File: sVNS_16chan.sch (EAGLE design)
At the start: 7 parts, among them IC1 EFM8SB10F8G-A-CSP16R, IC2 OPA990IDCKR, U1 NT3H2211W0FHKH, U2 LT8410EDC-1#TRMPBF, U3 MUX36S16IRSNR, U4 MUX36S16IRSNR

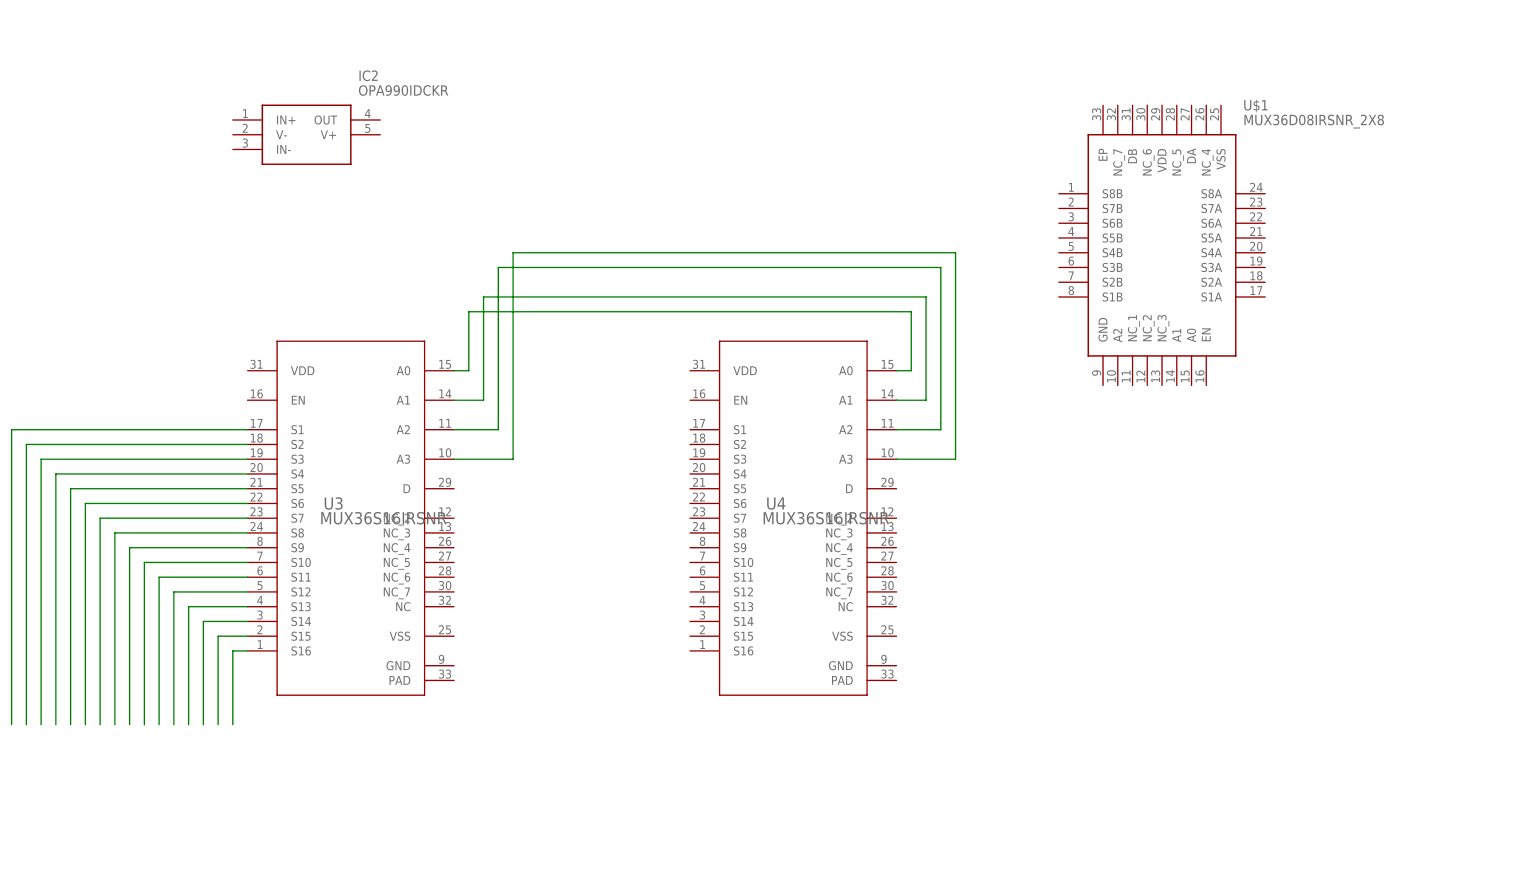
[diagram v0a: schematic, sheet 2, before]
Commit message: Draft of 2x MUX36S16 for output and 1x MUX36D08 for H-bridge
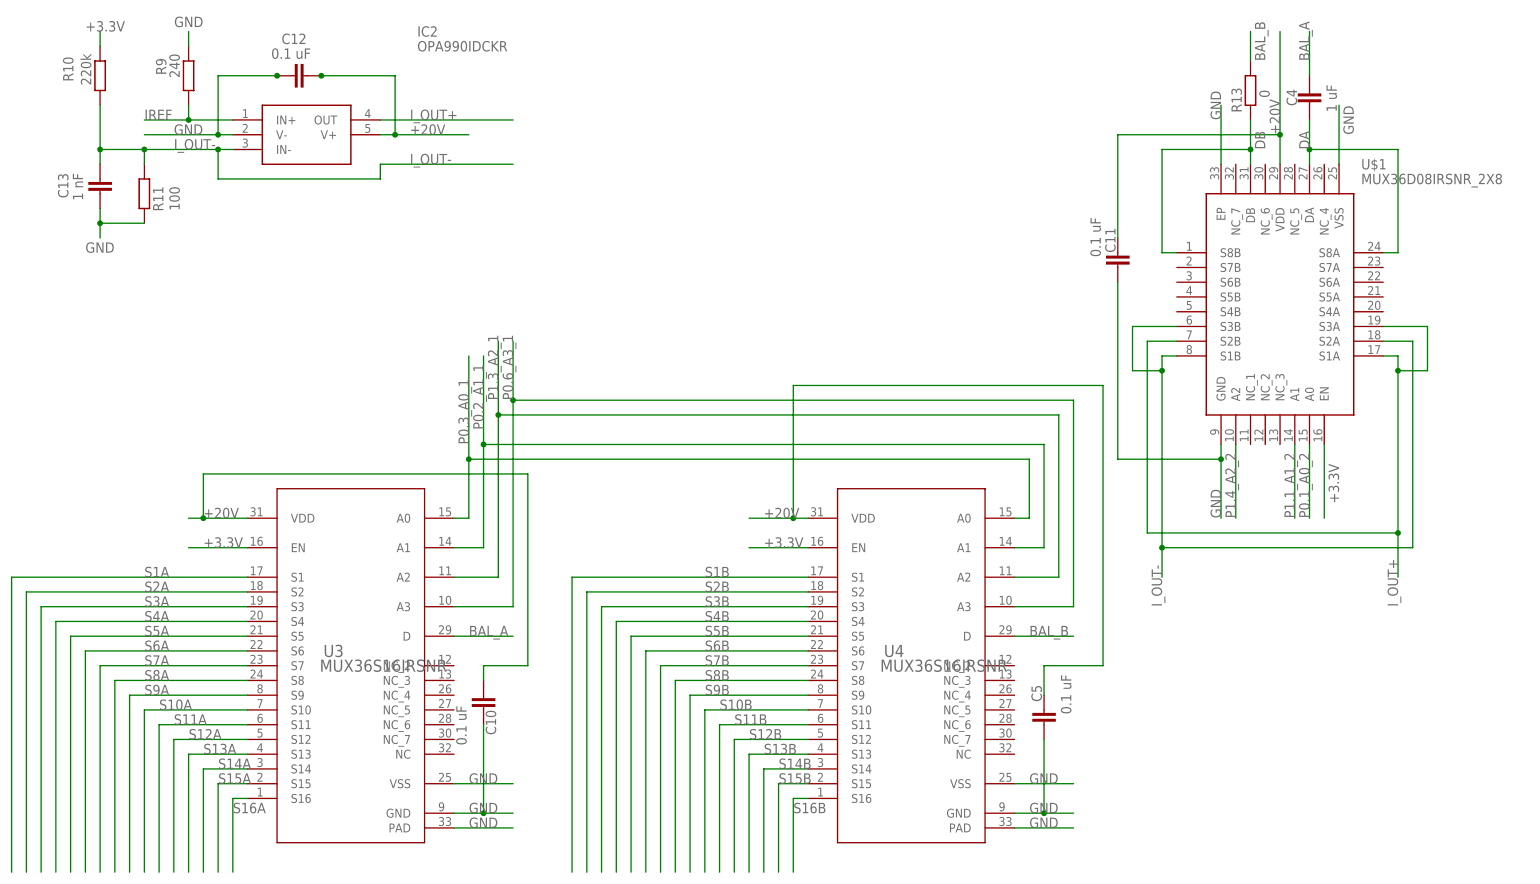
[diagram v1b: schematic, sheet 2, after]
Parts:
- added +20V_EXTERNAL_POWER: +20V external, pinhead:PINHD-1X2
- added +3.3V_EXTERNAL_POWER: +3.3V external, pinhead:PINHD-1X2
- added ANTENNA: Antenna connector, pinhead:PINHD-1X2
- added C1, C3: 2.2 uF, rcl:C-EUC0402
- added C10, C11, C12, C2, C5, C7: 0.1 uF, rcl:C-EUC0402
- added C13: 1 nF, rcl:C-EUC0402
- added C4, C8: 1 uF, rcl:C-EUC0402
- added C6: 82p, rcl:C-EUC0402
- added C9: 0.22u, rcl:C-EUC0402
- added L1: 47 uH, CustomLibVNS:0603PS-473KRC0603PS
- added R1: 487k, rcl:R-EU_R0603
- added R10: 220k, rcl:R-EU_R0402
- added R11: 100, rcl:R-EU_R0402
- added R13: 0, rcl:R-EU_R0402
- added R2: 511k, rcl:R-EU_R0603
- added R3: 1.3M, rcl:R-EU_R0402
- added R4: 100k, rcl:R-EU_R0402
- added R5, R6, R7: 10k, rcl:R-EU_R0402
- added R8: 1k, rcl:R-EU_R0402
- added R9: 240, rcl:R-EU_R0402
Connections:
- net N$1 renamed S16A
- net N$10 renamed S7A
- net N$11 renamed S6A
- net N$12 renamed S5A
- net N$13 renamed S4A
- net N$14 renamed S3A
- net N$15 renamed S2A
- net N$16 renamed S1A
- net N$2 renamed S15A
- net N$3 renamed S14A
- net N$4 renamed S13A
- net N$5 renamed S12A
- net N$6 renamed S11A
- net N$7 renamed S10A
- net N$8 renamed S9A
- net N$9 renamed S8A
- removed net N$17: U3.A0, U4.A0
- removed net N$18: U3.A1, U4.A1
- removed net N$19: U3.A2, U4.A2
- removed net N$20: U3.A3, U4.A3
- new net +20V: +20V_EXTERNAL_POWER.1, C10.1, C11.2, C3.1, C5.2, IC2.V+, U$1.VDD, U2.VOUT, U3.VDD, U4.VDD
- new net +20V1: C12.1
- new net +3.3V: +3.3V_EXTERNAL_POWER.1, C1.2, C7.2, C8.1, C9.1, IC1.VDD, L1.1, R10.1, R5.2, R6.2, R7.2, R8.1, U$1.EN, U1.VCC, U1.VOUT, U2.VCC, U3.EN, U4.EN
- new net BAL_A: C4.2, U3.D
- new net BAL_B: R13.2, U4.D
- new net DA: C4.1, U$1.DA, U$1.S8A
- new net DB: R13.1, U$1.DB, U$1.S8B
- new net FBP: R1.1, R2.2, U2.FBP
- new net FD: R7.1, U1.FD
- new net GND: +20V_EXTERNAL_POWER.2, +3.3V_EXTERNAL_POWER.2, C1.1, C10.2, C11.1, C13.1, C2.1, C3.2, C5.1, C7.1, C8.2, C9.2, IC1.GND, IC2.V-, R11.2, R2.1, R4.1, R9.1, U$1.EP, U$1.GND, U$1.VSS, U1.VSS, U2.EP, U2.GND, U3.GND, U3.PAD, U3.VSS, U4.GND, U4.PAD, U4.VSS
- new net GND1: C12.2
- new net IREF: IC2.IN+, R9.2
- new net I_OUT+: IC2.OUT, R3.2, U$1.S1A, U$1.S2B, U$1.S3A
- new net I_OUT-: C13.2, IC2.IN-, R10.2, R11.1, U$1.S1B, U$1.S2A, U$1.S3B
- new net N$56: ANTENNA.1, C6.1, U1.LA
- new net N$57: ANTENNA.2, C6.2, U1.LB
- new net N$58: C2.2, U2.CAP
- new net P0.0_SMBUS_SDA: IC1.P0.0, R5.1, U1.SDA
- new net P0.1_A0_2: IC1.P0.1, U$1.A0
- new net P0.2_A1_1: IC1.P0.2, U3.A1, U4.A1
- new net P0.3_A0_1: IC1.P0.3, U3.A0, U4.A0
- new net P0.4_SMBUS_SCL: IC1.P0.4, R6.1, U1.SCL
- new net P0.5_ADC: IC1.P0.5, R3.1, R4.2
- new net P0.6_A3_1: IC1.P0.6, U3.A3, U4.A3
- new net P0.7_IREF: IC1.P0.7
- new net P1.0_SHDN: IC1.P1.0, U2.!SHDN
- new net P1.1_A1_2: IC1.P1.1, U$1.A1
- new net P1.3_A2_1: IC1.P1.3, U3.A2, U4.A2
- new net P1.4_A2_2: IC1.P1.4, U$1.A2
- new net P2.7_/_C2D: IC1.P2.7_/_C2D
- new net RSTB_/_C2CK: IC1.RSTB_/_C2CK, R8.2
- new net S10B: U4.S10
- new net S11B: U4.S11
- new net S12B: U4.S12
- new net S13B: U4.S13
- new net S14B: U4.S14
- new net S15B: U4.S15
- new net S16B: U4.S16
- new net S1B: U4.S1
- new net S2B: U4.S2
- new net S3B: U4.S3
- new net S4B: U4.S4
- new net S5B: U4.S5
- new net S6B: U4.S6
- new net S7B: U4.S7
- new net S8B: U4.S8
- new net S9B: U4.S9
- new net SW: L1.2, U2.SW
- new net VREF: R1.2, U2.VREF
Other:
- note added: "External power supllies"
- moved on the sheet: IC1, U$1, U3, U4

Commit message: Schematic to submit to Enrico #1
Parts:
- added +20V_CHECK: Converted voltage, pinhead:PINHD-1X2
- added +3.3V_CHECK: Harvested voltage/NT3H, pinhead:PINHD-1X2
- added BAL_A: BAL_A check, pinhead:PINHD-1X2
- added BAL_B: BAL_B check, pinhead:PINHD-1X2
- added DEBUG_N_2510_SOCKET: N2510-6002RB, N2510-6002RB:N2510-6002RB
- added EFM8_VDD: EFM8 check, pinhead:PINHD-1X2
- added GROUND_CONNECTION: GND, pinhead:PINHD-1X2
- added I_OUT+: I_out+ check, pinhead:PINHD-1X2
- added I_OUT-: I_out- check, pinhead:PINHD-1X2
- added I_REF: IREF check, pinhead:PINHD-1X2
- added LT8410_VCC: LT8410 check, pinhead:PINHD-1X2
- added MUX36D08_VDD: MUX36D08 check, pinhead:PINHD-1X2
- added MUX36S16_A, MUX36S16_B: MUX36S16 check, pinhead:PINHD-1X2
- added OPA990_V+: OPA990 check, pinhead:PINHD-1X2
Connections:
- net N$56 renamed LA
- net N$57 renamed LB
- new net N$1: C7.2, C8.1, EFM8_VDD.2, R8.1
- new net N$2: LT8410_VCC.2, U2.VCC
- new net N$3: I_OUT+.2
- new net N$4: I_OUT-.1
- net +20V: now also +20V_CHECK.1, +20V_CHECK.2, MUX36D08_VDD.1, MUX36D08_VDD.2, MUX36S16_A.1, MUX36S16_A.2, MUX36S16_B.1, MUX36S16_B.2, OPA990_V+.1, OPA990_V+.2
- net +3.3V: now also +3.3V_CHECK.1, +3.3V_CHECK.2, EFM8_VDD.1, LT8410_VCC.1; no longer C7.2, C8.1, R8.1, U$1.EN, U2.VCC, U3.EN, U4.EN
- net BAL_A: now also BAL_A.1, BAL_A.2
- net BAL_B: now also BAL_B.1, BAL_B.2
- net GND: now also DEBUG_N_2510_SOCKET.2
- net I_OUT+: now also I_OUT+.1
- net I_OUT-: now also I_OUT-.2
- net P0.7_IREF: now also I_REF.1, I_REF.2
- net P1.0_SHDN: now also U$1.EN, U3.EN, U4.EN
- net P2.7_/_C2D: now also DEBUG_N_2510_SOCKET.4
- net RSTB_/_C2CK: now also DEBUG_N_2510_SOCKET.7
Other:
- note added: "Debug connector"
- moved on the sheet: ANTENNA, C11, C4, C6, C9, R13, R5, R6, R7, U$1, U1

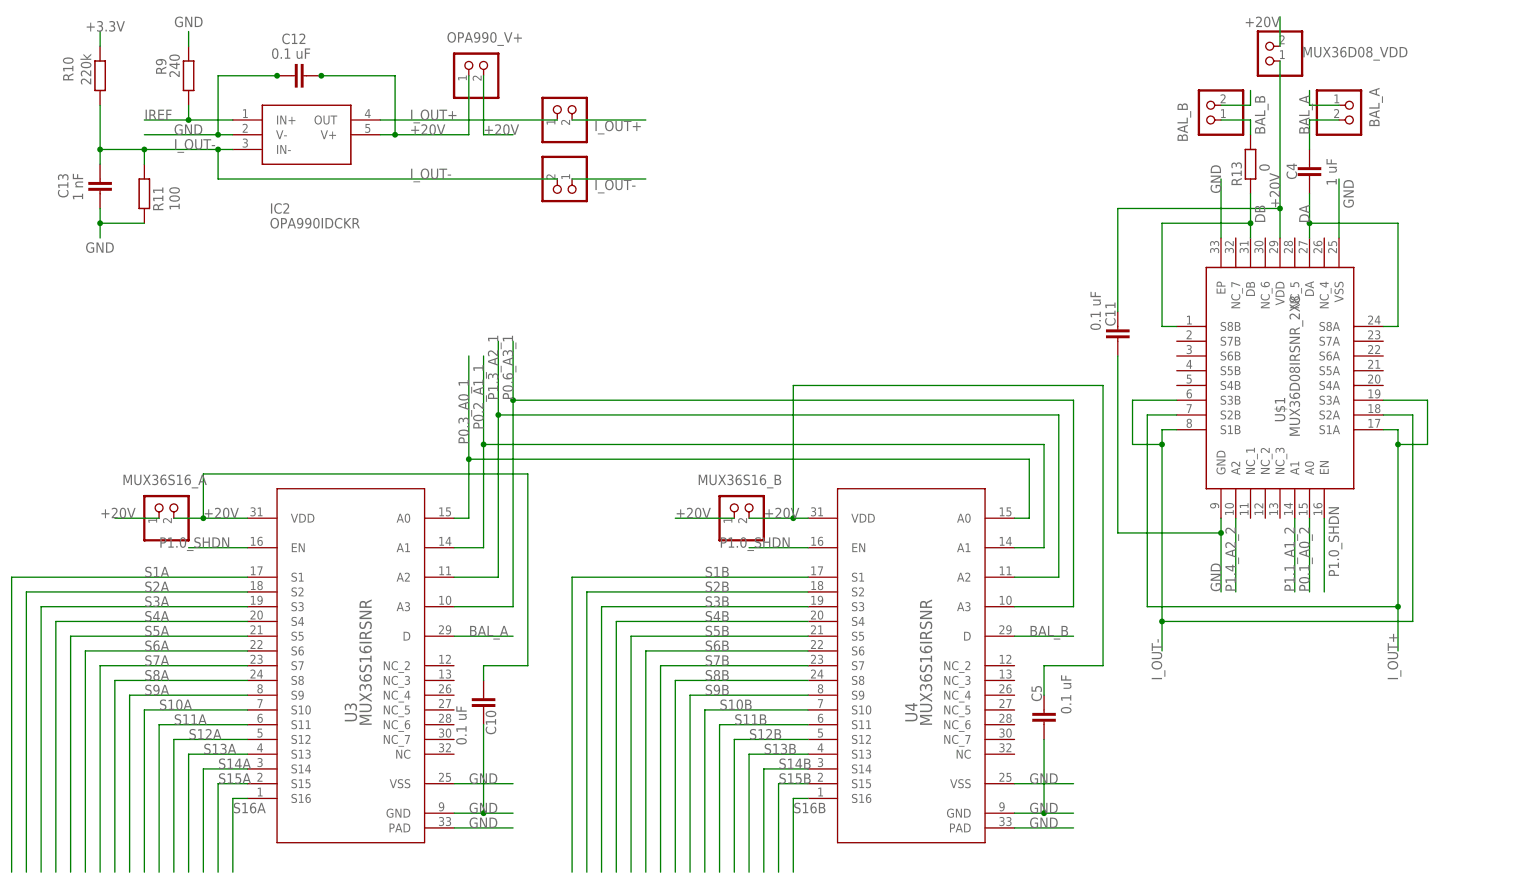
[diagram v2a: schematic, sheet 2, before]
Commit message: #1 submission to Enrico - fixed pin names
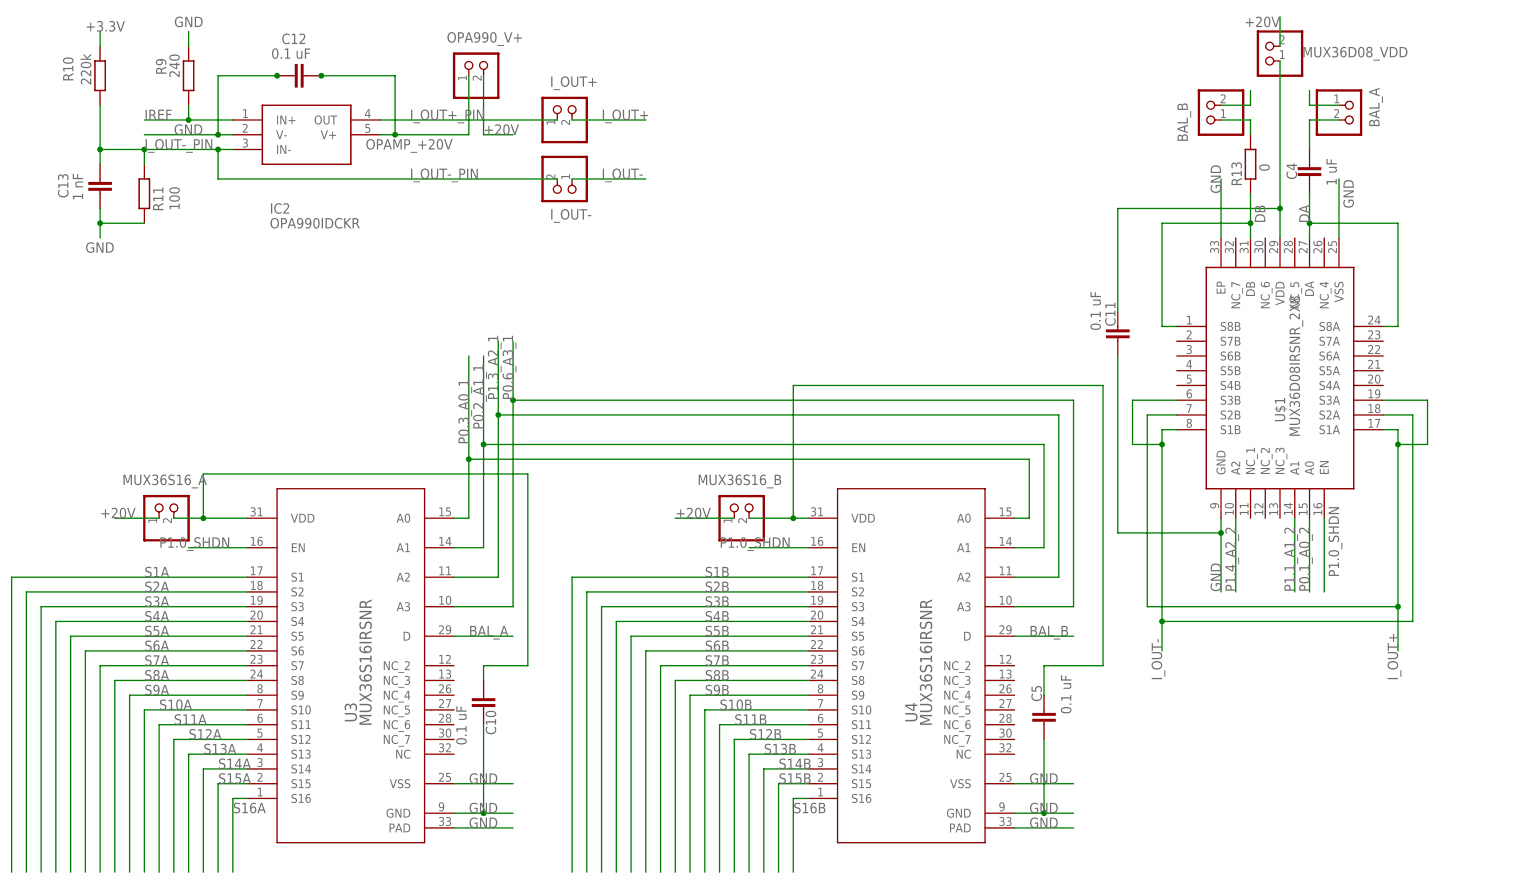
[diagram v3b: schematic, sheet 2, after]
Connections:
- net N$2 renamed +3.3V_LT8410_VCC
- removed net N$1: C7.2, C8.1, EFM8_VDD.2, R8.1
- removed net N$3: I_OUT+.2
- removed net N$4: I_OUT-.1
- new net +20V_PIN: +20V_CHECK.2
- new net +3.3V_PIN: +3.3V_CHECK.2
- new net +3.3V_VDD: EFM8_VDD.1, IC1.VDD
- new net BAL_A_PIN: BAL_A.2, C4.2
- new net BAL_B_PIN: BAL_B.1, R13.2
- new net I_OUT+_PIN: IC2.OUT, I_OUT+.1
- new net I_OUT-_PIN: C13.2, IC2.IN-, I_OUT-.2, R10.2, R11.1
- new net MUX36D08_+20V: C11.2, MUX36D08_VDD.1, U$1.VDD
- new net MUX36S16A+20V: C10.1, MUX36S16_A.2, U3.VDD
- new net MUX36S16B_+20V: C5.2, MUX36S16_B.2, U4.VDD
- new net OPAMP_+20V: IC2.V+, OPA990_V+.1
- new net P0.7_IREF_PIN: IC1.P0.7, I_REF.2
- net +20V: no longer +20V_CHECK.2, C10.1, C11.2, C5.2, IC2.V+, MUX36D08_VDD.1, MUX36S16_A.2, MUX36S16_B.2, OPA990_V+.1, U$1.VDD, U3.VDD, U4.VDD
- net +3.3V: now also C7.2, C8.1, EFM8_VDD.2, R8.1; no longer +3.3V_CHECK.2, EFM8_VDD.1, IC1.VDD
- net BAL_A: no longer BAL_A.2, C4.2
- net BAL_B: no longer BAL_B.1, R13.2
- net GND: now also GROUND_CONNECTION.1, GROUND_CONNECTION.2
- net I_OUT+: now also I_OUT+.2; no longer IC2.OUT, I_OUT+.1
- net I_OUT-: now also I_OUT-.1; no longer C13.2, IC2.IN-, I_OUT-.2, R10.2, R11.1
- net P0.7_IREF: no longer IC1.P0.7, I_REF.2

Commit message: Modified schematic as per Enricos suggestions
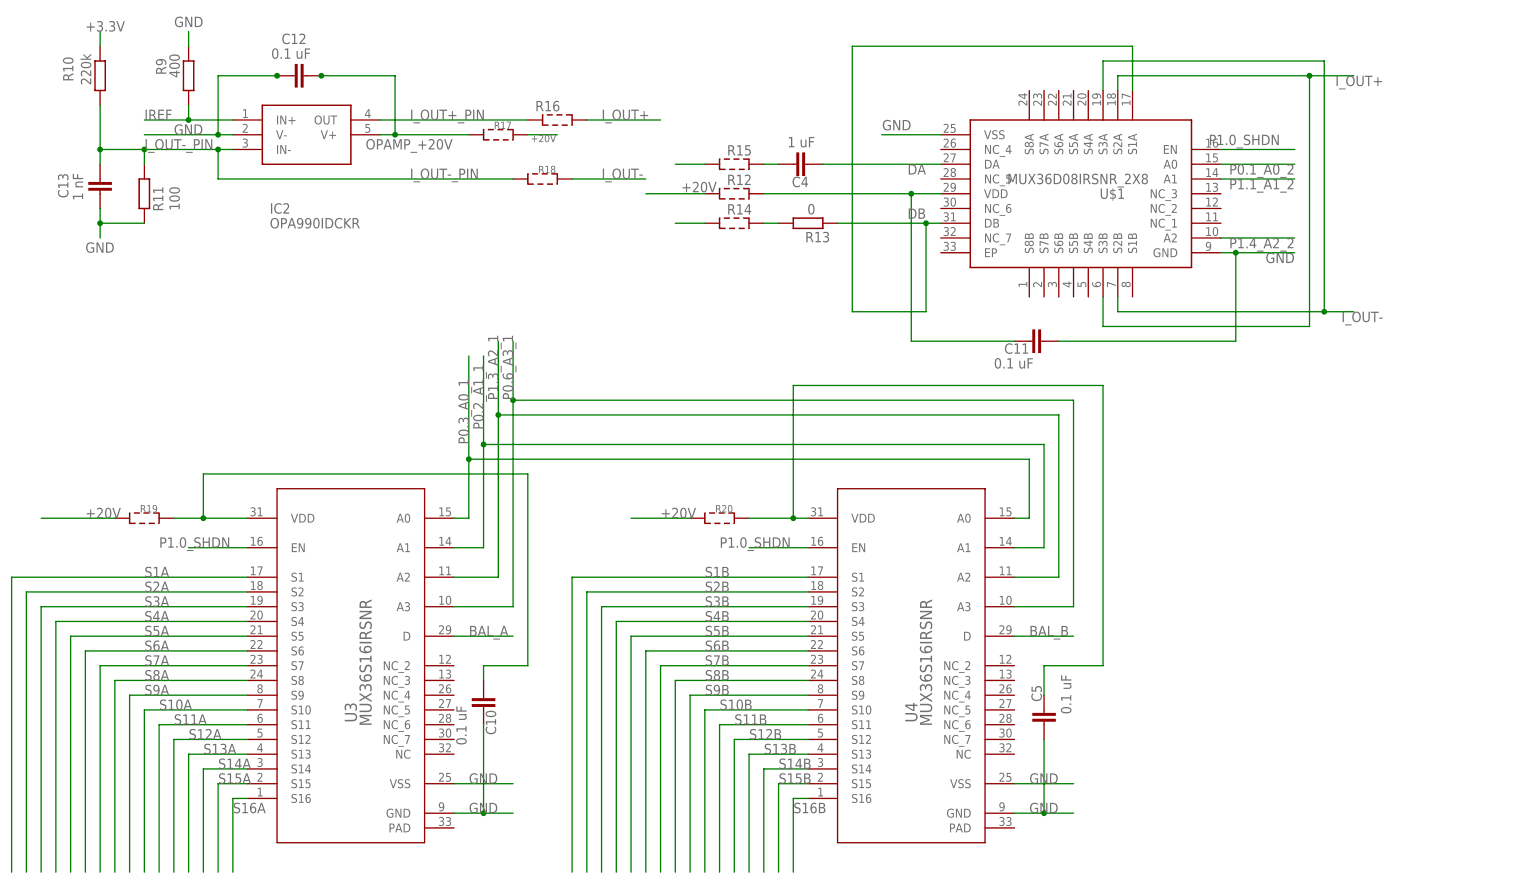
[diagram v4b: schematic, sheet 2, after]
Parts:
- removed +20V_CHECK: Converted voltage, pinhead:PINHD-1X2
- removed +3.3V_CHECK: Harvested voltage/NT3H, pinhead:PINHD-1X2
- removed BAL_A: BAL_A check, pinhead:PINHD-1X2
- removed BAL_B: BAL_B check, pinhead:PINHD-1X2
- removed EFM8_VDD: EFM8 check, pinhead:PINHD-1X2
- removed I_OUT+: I_out+ check, pinhead:PINHD-1X2
- removed I_OUT-: I_out- check, pinhead:PINHD-1X2
- removed I_REF: IREF check, pinhead:PINHD-1X2
- removed LT8410_VCC: LT8410 check, pinhead:PINHD-1X2
- removed MUX36D08_VDD: MUX36D08 check, pinhead:PINHD-1X2
- removed MUX36S16_A, MUX36S16_B: MUX36S16 check, pinhead:PINHD-1X2
- removed OPA990_V+: OPA990 check, pinhead:PINHD-1X2
- added C14: 0.1 uF, rcl:C-EUC0402
- added R12, R14, R15, R16, R17, R18, R19, R20, R21, R22, R23, R24, R25: (no value), sVNS_16chan_lib:SMD_PADSR0402
- R9: value 240 -> 400
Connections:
- net +20V: now also R12.1, R17.2, R19.1, R20.1, R24.1; no longer +20V_CHECK.1, MUX36D08_VDD.2, MUX36S16_A.1, MUX36S16_B.1, OPA990_V+.2
- net +20V_PIN: now also R24.2; no longer +20V_CHECK.2
- net +3.3V: now also R21.2, R23.2, R25.1, U2.VCC; no longer +3.3V_CHECK.1, C1.2, EFM8_VDD.2, LT8410_VCC.1
- net +3.3V_LT8410_VCC: now also C1.2, R23.1; no longer LT8410_VCC.2, U2.VCC
- net +3.3V_PIN: now also R25.2; no longer +3.3V_CHECK.2
- net +3.3V_VDD: now also R21.1; no longer EFM8_VDD.1
- net BAL_A: now also R15.1; no longer BAL_A.1
- net BAL_A_PIN: now also R15.2; no longer BAL_A.2
- net BAL_B: now also R14.1; no longer BAL_B.2
- net BAL_B_PIN: now also R14.2; no longer BAL_B.1
- net DA: no longer U$1.S8A
- net DB: now also U$1.S1A; no longer U$1.S8B
- net FBP: now also C14.2
- net GND: now also C14.1; no longer U$1.EP, U3.PAD, U4.PAD
- net I_OUT+: now also R16.2, U$1.S2A, U$1.S3B; no longer I_OUT+.2, U$1.S1A, U$1.S2B, U$1.S3A
- net I_OUT+_PIN: now also R16.1; no longer I_OUT+.1
- net I_OUT-: now also R18.2, U$1.S2B, U$1.S3A; no longer I_OUT-.1, U$1.S1B, U$1.S2A, U$1.S3B
- net I_OUT-_PIN: now also R18.1; no longer I_OUT-.2
- net MUX36D08_+20V: now also R12.2; no longer MUX36D08_VDD.1
- net MUX36S16A+20V: now also R19.2; no longer MUX36S16_A.2
- net MUX36S16B_+20V: now also R20.2; no longer MUX36S16_B.2
- net OPAMP_+20V: now also R17.1; no longer OPA990_V+.1
- net P0.7_IREF: now also R22.1; no longer I_REF.1
- net P0.7_IREF_PIN: now also R22.2; no longer I_REF.2
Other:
- note added: "Generated power check"
- moved on the sheet: C1, C11, C4, R13, U$1
